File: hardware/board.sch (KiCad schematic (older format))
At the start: 41 parts, among them J1 Conn_01x04_Female, J2 Conn_01x04_Female, J3 Conn_01x04_Female, J4 Conn_01x06_Female, J5 Conn_01x14, J6 Micro_SD_Card, P1 USB_C_Plug_USB2.0, SW1 SW_Push, SW2 SW_Push, SW3 SW_Push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

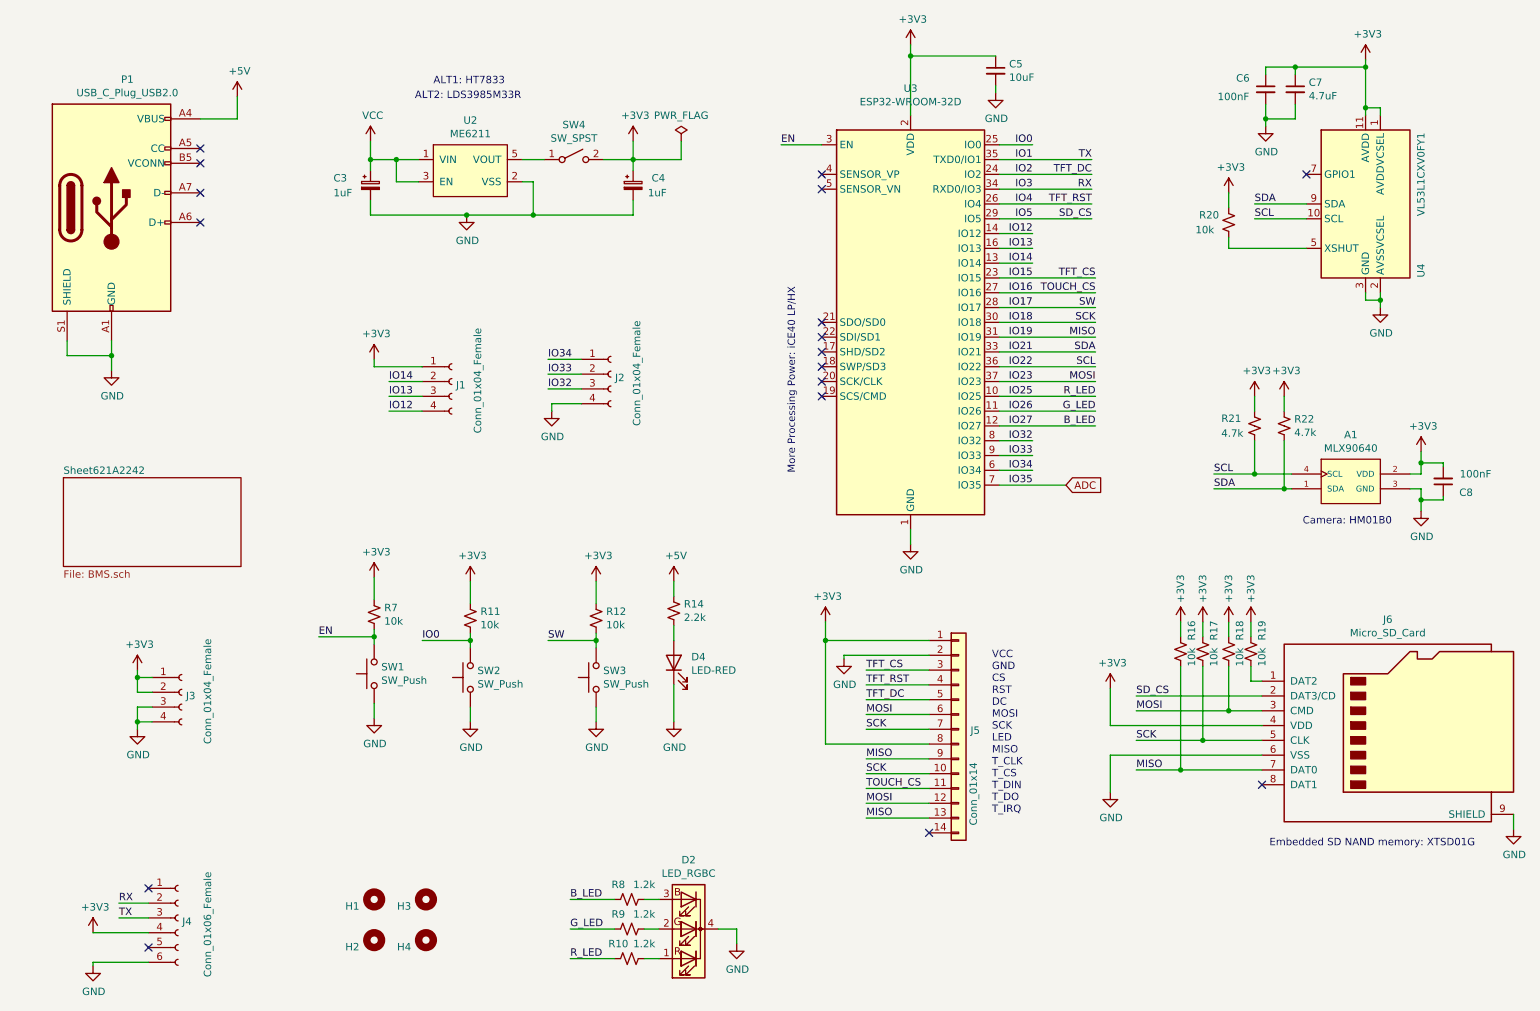
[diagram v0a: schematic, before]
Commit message: Folder reorganized: hardware
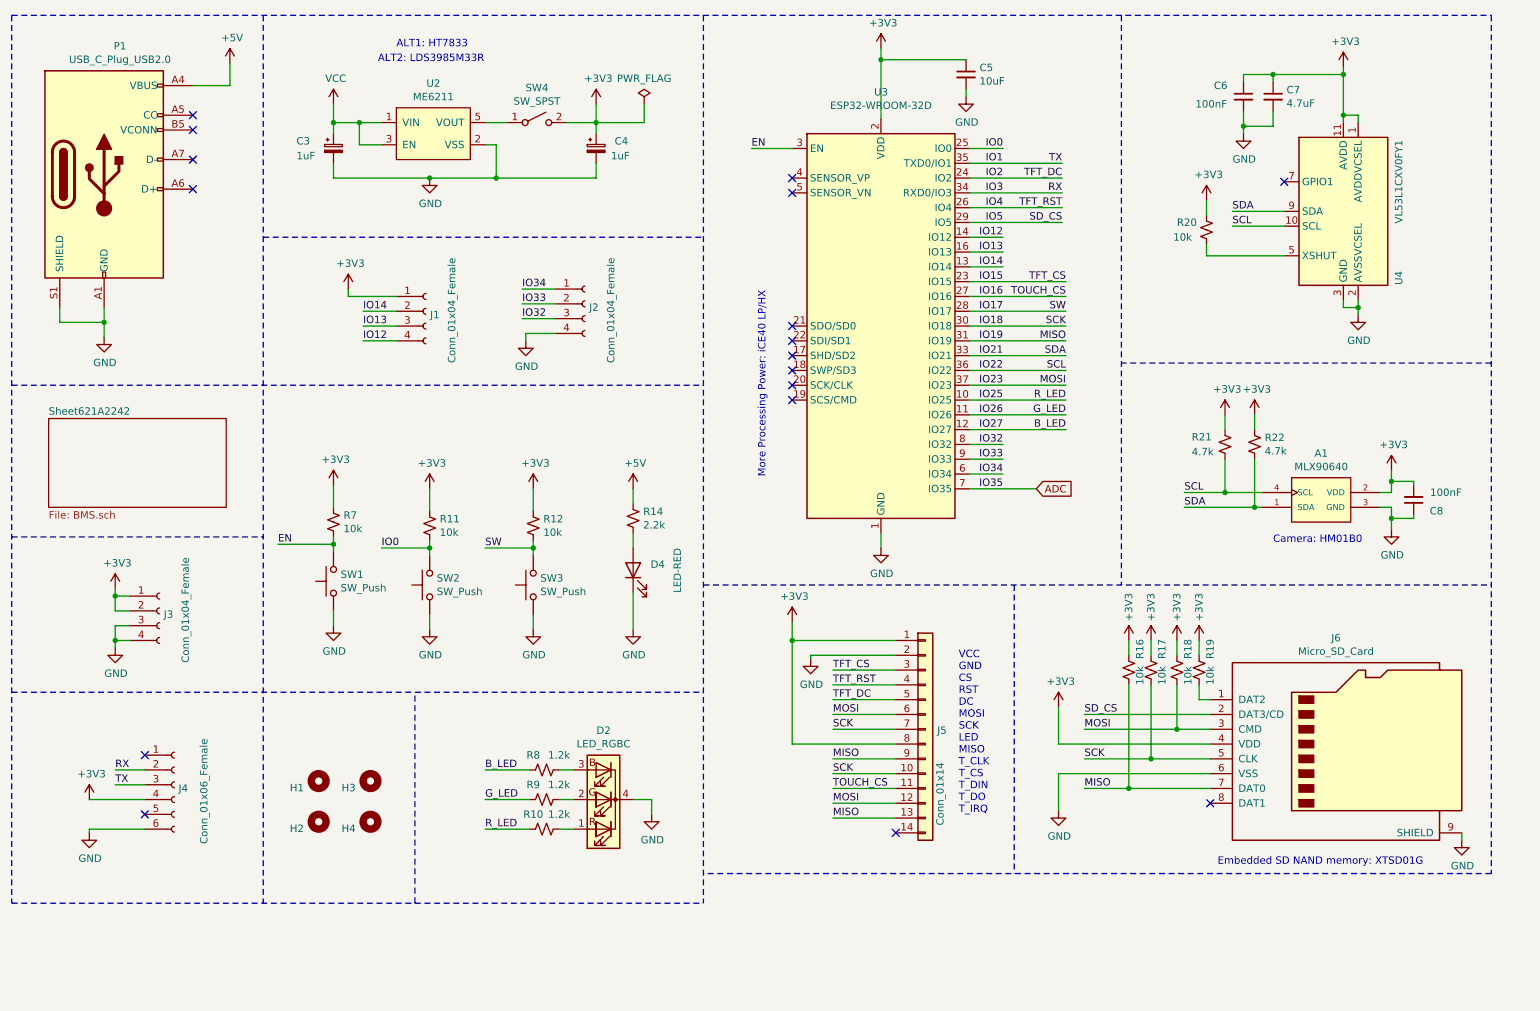
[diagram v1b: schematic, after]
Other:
- moved on the sheet: A1, C3, C4, C5, C6, C7, C8, D2, D4, H1, H2, H3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
